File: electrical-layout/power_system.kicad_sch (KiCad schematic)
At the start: 12 parts, among them SW1 SW_Push, U16 NO Switch, U17 NC Switch, U2 NO Switch, U4 NO Switch

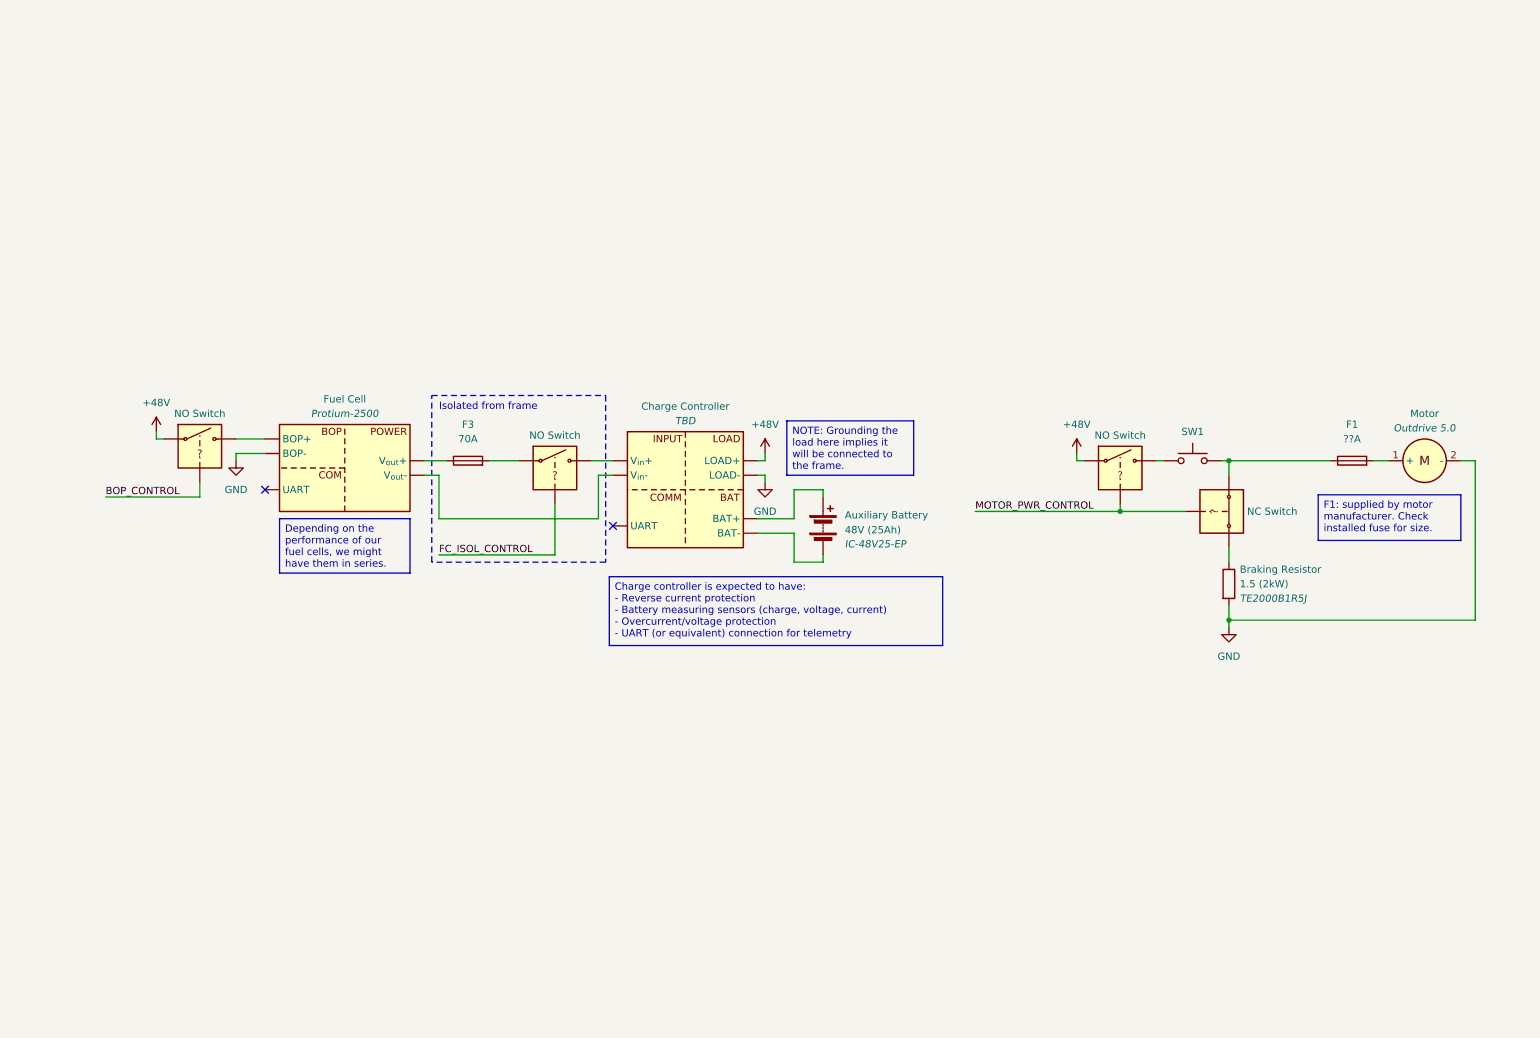
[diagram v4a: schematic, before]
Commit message: layout-2025: add power control pcb
This PCB is used to:
- Control power MOSFETs (as switches)
- Read UART data from fuel cell(s) and charge controller
- Communicate over the CAN bus

Unknown switches were replaced with MOSFETs in the power layout.
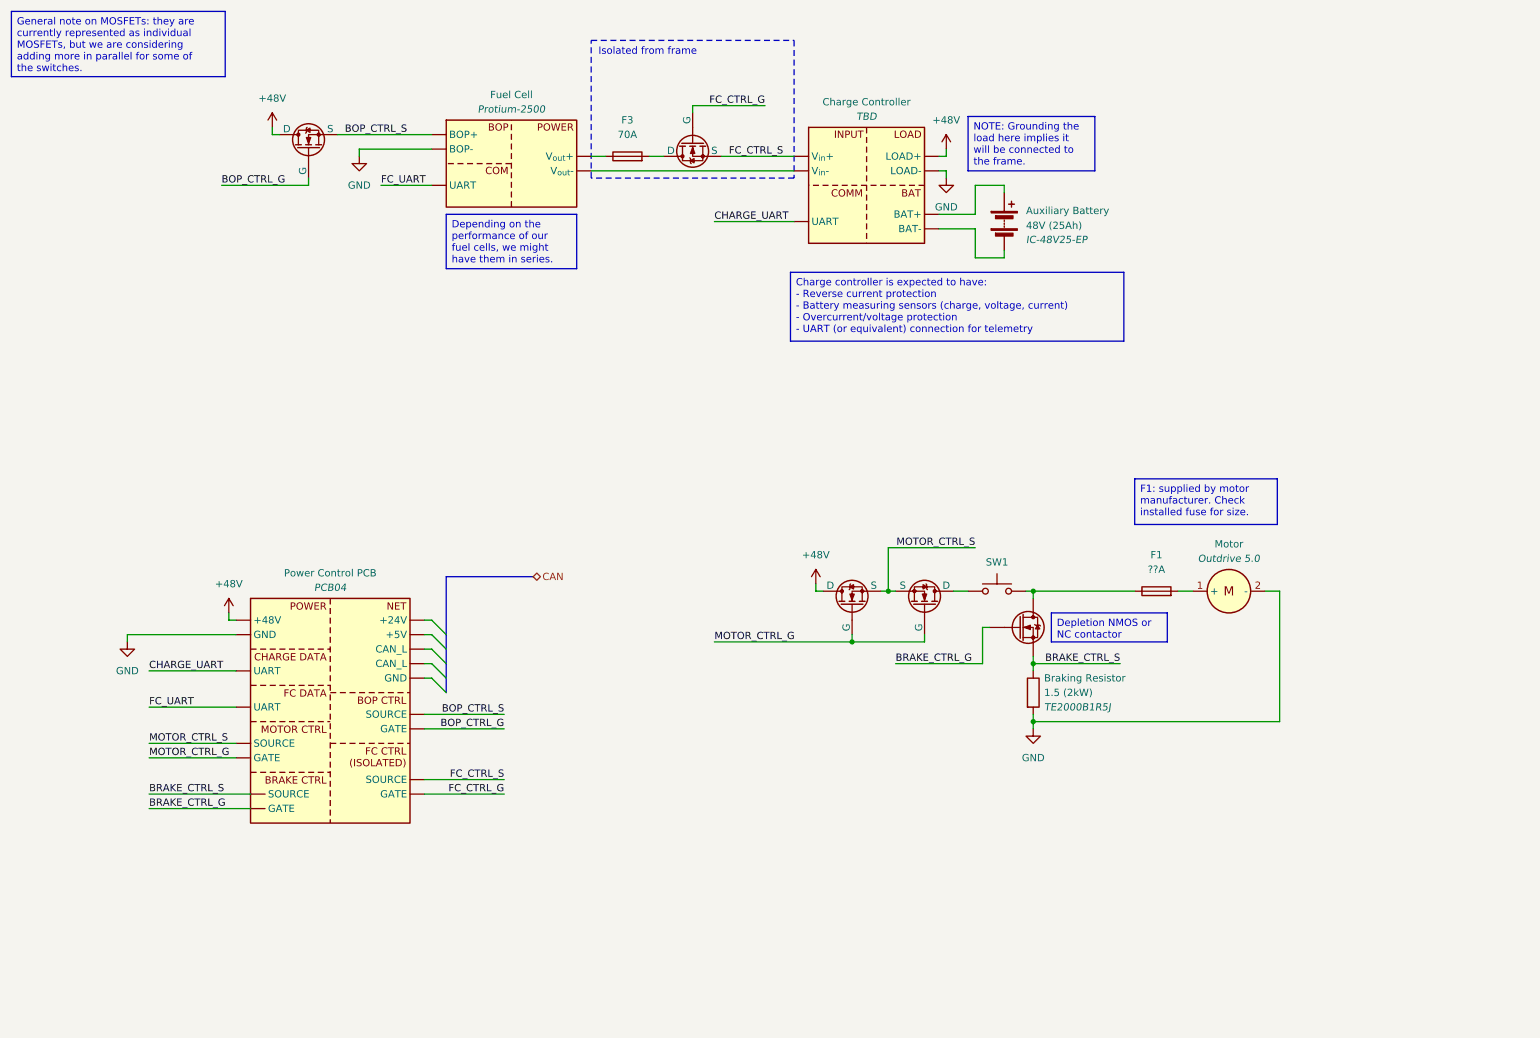
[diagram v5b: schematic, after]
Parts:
- removed U16, U2, U4: NO Switch, symbol Exocet:VC_Switch_NO
- removed U17: NC Switch, symbol Exocet:VC_Switch_NC
- added Q1: Q_NMOS_Depletion, symbol Device:Q_NMOS_Depletion
- added Q2, Q3, Q4, Q5: NMOS, symbol Simulation_SPICE:NMOS
- added U4: ~, symbol Exocet:Power_Control_Pcb
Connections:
- net +48V: now also Q2.1 (D), Q4.1 (D), U4. (GATE)
- net GND: now also U4. (GATE)
- net BRAKE_CTRL_S: now reaches R1.1
- net BRAKE_CTRL_S: now also Q1.S, U4. (GATE)
- net at F1.1, SW1.2: now also Q1.D
- net at SW1.1: now also Q3.1 (D)
- net at F3.2: now also Q5.1 (D)
- new net: U19. (BAT-), U3. (V_{out}-)
- new net BOP_CTRL_G: Q4.2 (G), U4. (GATE)
- new net BOP_CTRL_S: Q4.3 (S), U3. (V_{out}-), U4. (GATE)
- new net BRAKE_CTRL_G: Q1.G, U4. (GATE)
- new net CHARGE_UART: U19. (BAT-), U4. (GATE)
- new net FC_CTRL_G: Q5.2 (G), U4. (GATE)
- new net FC_CTRL_S: Q5.3 (S), U19. (BAT-), U4. (GATE)
- new net FC_UART: U3. (V_{out}-), U4. (GATE)
- new net MOTOR_CTRL_G: Q2.2 (G), Q3.2 (G), U4. (GATE)
- new net MOTOR_CTRL_S: Q2.3 (S), Q3.3 (S), U4. (GATE)
- no-connect marks 2 -> 0
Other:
- moved on the sheet: F1, F3, SW1
